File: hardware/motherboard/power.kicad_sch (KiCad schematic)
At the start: 23 parts, among them J1 9-28V, U10 LM2576SX-5.0, U2 AMS1117-3.3

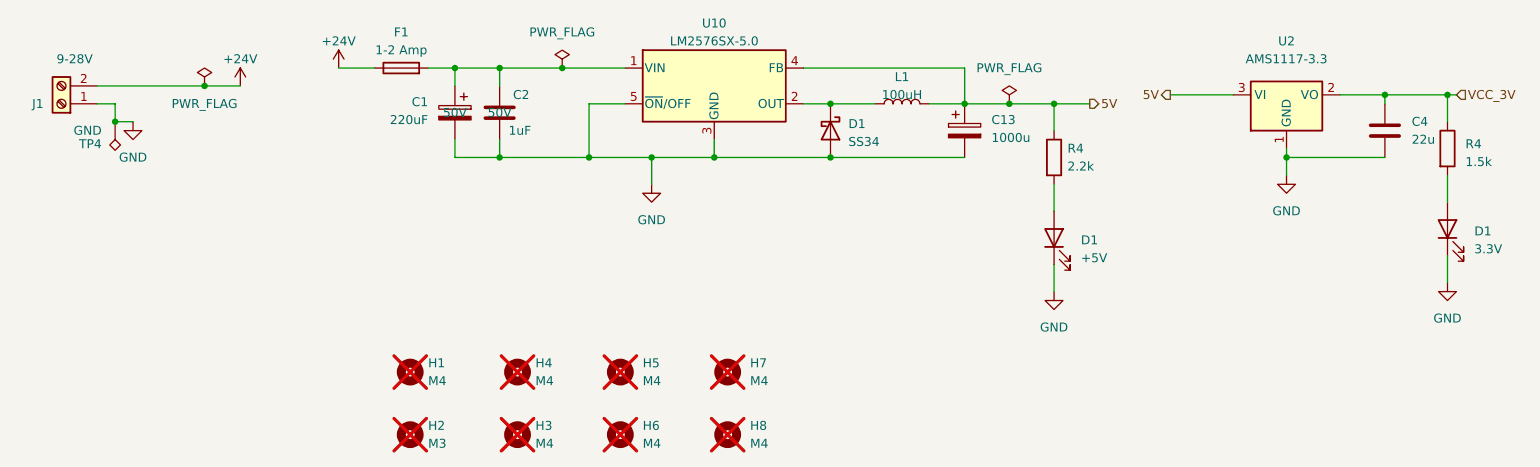
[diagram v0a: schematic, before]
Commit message: Update to KiCAD 10
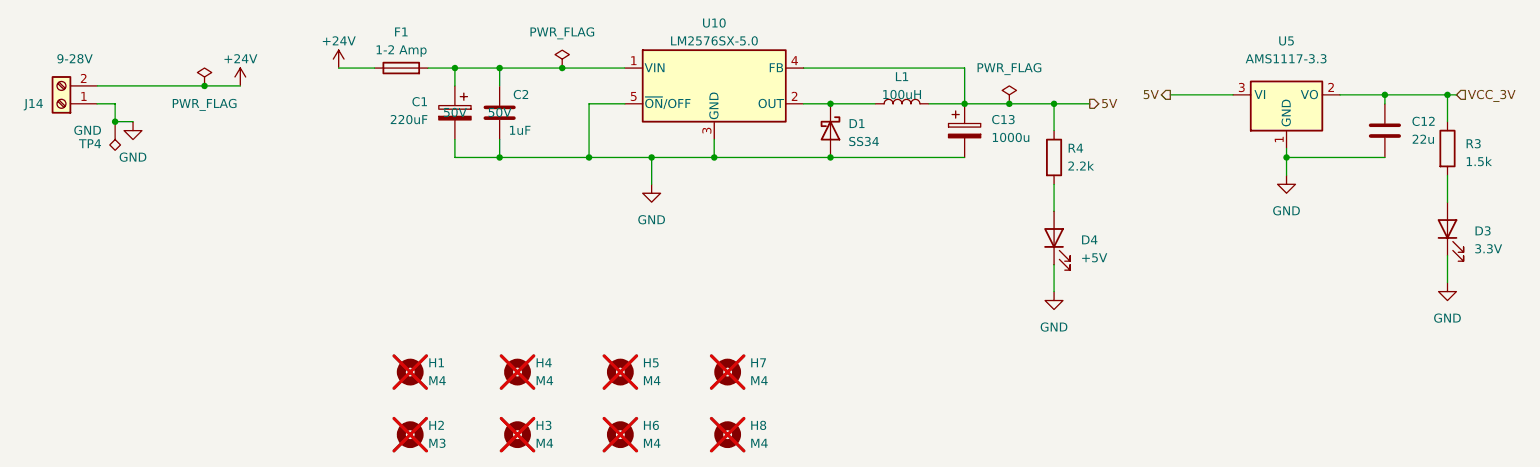
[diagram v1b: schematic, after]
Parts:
- renumbered C4 to C12, D1 to D3, D1 to D4, J1 to J14, R4 to R3, U2 to U5
